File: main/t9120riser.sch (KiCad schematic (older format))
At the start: 33 parts, among them J1 PCIeX16, J2 PCIeX8, J3 M.2 ACTIVITY LED, J4 MDT420M03001, J5 X4MEZZ_HSA, J6 X4MEZZ_MPA, J7 X4MEZZ_MPB, J8 X4MEZZ_HSB, U1 ZL40264

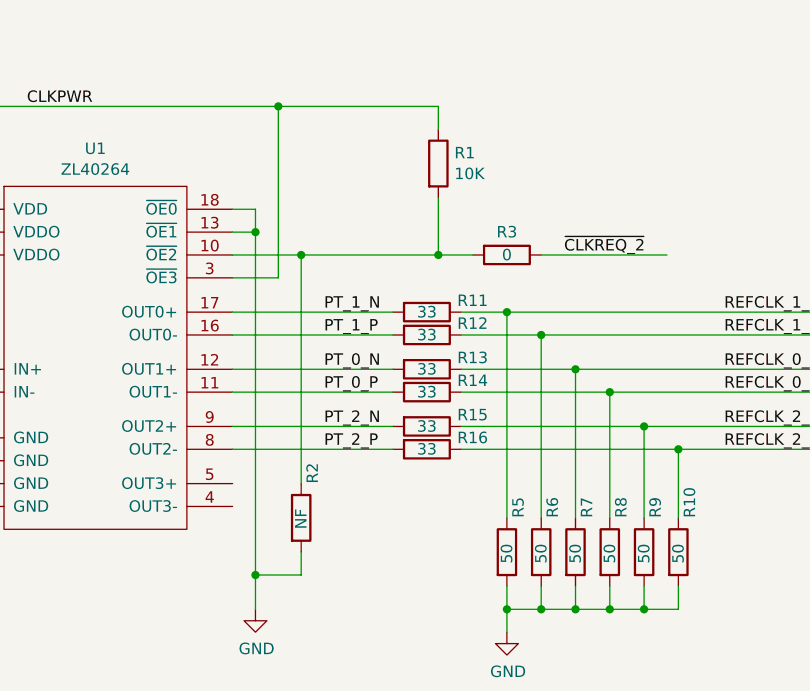
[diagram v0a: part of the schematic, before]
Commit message: Added PDFs
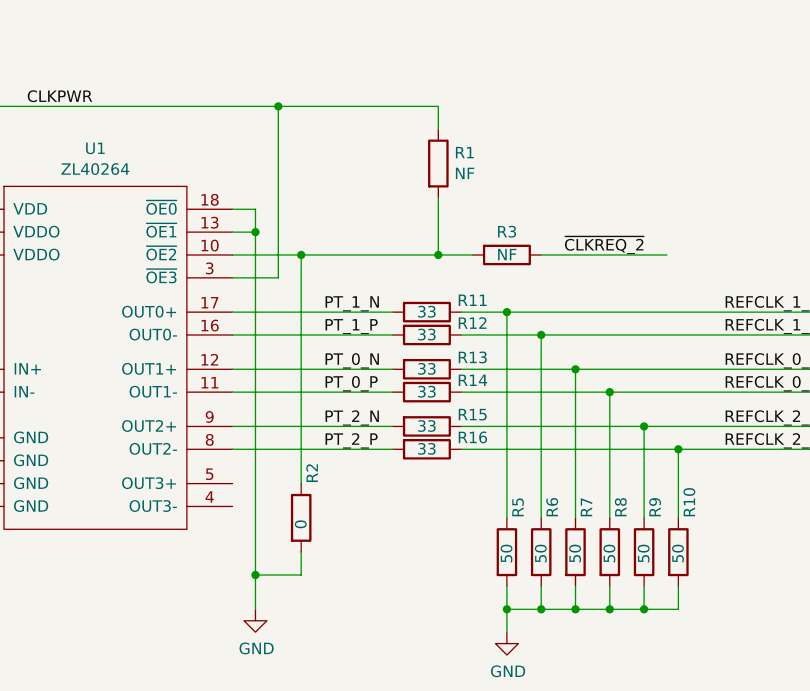
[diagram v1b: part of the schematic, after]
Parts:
- R1: value 10K -> NF
- R2: value NF -> 0
- R3: value 0 -> NF
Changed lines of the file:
@@
 P 9450 9150
 F 0 "R3" V 9350 9150 50  0000 C CNN
-F 1 "0" V 9450 9150 50  0000 C CNN
+F 1 "NF" V 9450 9150 50  0000 C CNN
 F 2 "Resistor_SMD:R_0603_1608Metric" V 9380 9150 50  0001 C CNN
 F 3 "~" H 9450 9150 50  0001 C CNN
@@
 P 8550 10300
 F 0 "R2" V 8600 10450 50  0000 L CNN
-F 1 "NF" V 8550 10250 50  0000 L CNN
+F 1 "0" V 8550 10250 50  0000 L CNN
 F 2 "Resistor_SMD:R_0603_1608Metric" V 8480 10300 50  0001 C CNN
 F 3 "~" H 8550 10300 50  0001 C CNN
@@
 P 9150 8750
 F 0 "R1" H 9220 8796 50  0000 L CNN
-F 1 "10K" H 9220 8705 50  0000 L CNN
+F 1 "NF" H 9220 8705 50  0000 L CNN
 F 2 "Resistor_SMD:R_0603_1608Metric" V 9080 8750 50  0001 C CNN
 F 3 "~" H 9150 8750 50  0001 C CNN
